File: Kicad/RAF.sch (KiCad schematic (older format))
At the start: 22 parts, among them P1 Power, P2 Analog, P3 Digital, P4 Digital, P5 CONN_01X01, P6 CONN_01X01, P7 CONN_01X01, P8 CONN_01X01, Q1 FDG1024NZ, U1 RGB_WS2811B

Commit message: add sot23-6 footprint, fix drc errors
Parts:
- removed Q1: FDG1024NZ, TO_SOT_Packages_SMD:SOT-363_SC-70-6, symbol FDG1024NZ
- added C1: 10uF 25V, symbol C
- added C2: 100n, symbol C
- added C3: 82pF, symbol C
- added C4, C5: 22uF, symbol C
- added J3: SOL, symbol CONN_01X02
- added J5: PUMP, symbol CONN_01X02
- added J6: WS2811-OUT, symbol CONN_01X03
- added L1: 12uH, symbol L
- added Q1: FDC6305N, TO_SOT_Packages_SMD:SuperSOT-6, symbol FDC6305N
- added R3, R7: 100K, symbol R
- added R4: 11K, symbol R
- added R5, R6: 10K, symbol R
- added S1: SPST-M, symbol SPST-M
- added U2: TPS54302, symbol TPS54302
- gave numbers to parts that had none: 3
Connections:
- wire segments 81 -> 130
- no-connect marks 5 -> 16
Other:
- note added: "Air pump control\n"
- note added: "Servo (6V - 2A) power supply"
- note added: "Solenoid Control"
- moved on the sheet: J1, J2, J4, JOY1, LDR1, P1, P2, P3, P4, P5, P6, P7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

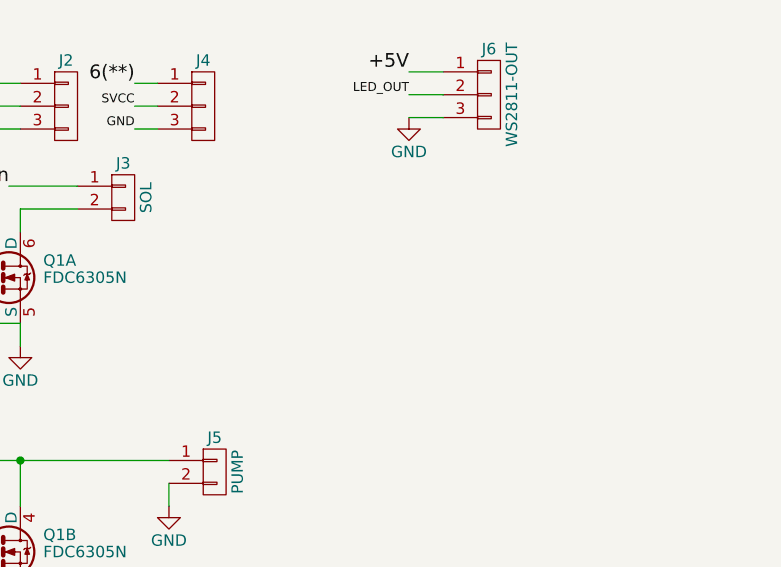
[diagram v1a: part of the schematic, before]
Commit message: add i2c header
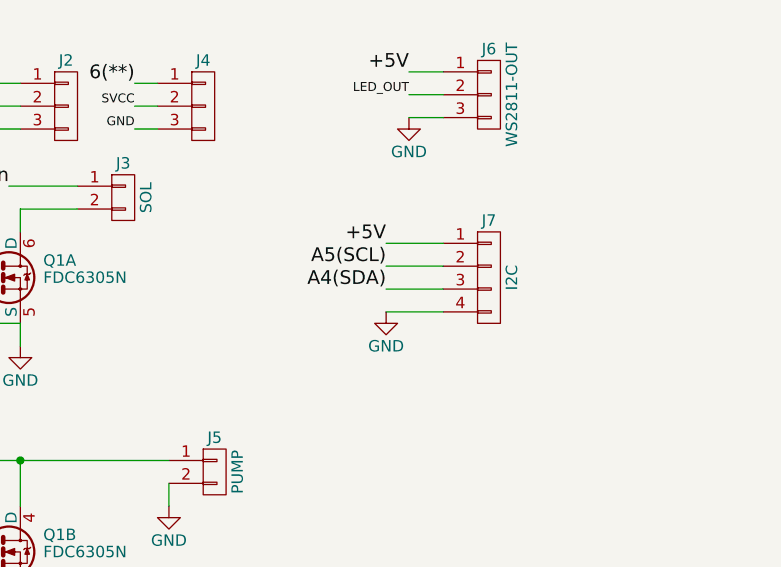
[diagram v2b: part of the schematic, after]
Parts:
- added J7: I2C, symbol CONN_01X04
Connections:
- net +5V: now also J7.1 (P1)
- net A4(SDA): now also J7.3 (P3)
- net A5(SCL): now also J7.2 (P2)
- net GND: now also J7.4 (P4)
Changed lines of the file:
@@
 $EndComp
 Connection ~ 8300 4550
+$Comp
+L CONN_01X04 J7
+U 1 1 59779033
+P 9250 1850
+F 0 "J7" H 9250 2100 50  0000 C CNN
+F 1 "I2C" V 9350 1850 50  0000 C CNN
+F 2 "" H 9250 1850 50  0001 C CNN
+F 3 "" H 9250 1850 50  0001 C CNN
+	1    9250 1850
+	1    0    0    -1
+$EndComp
+Wire Wire Line
+	8800 1700 9050 1700
+Wire Wire Line
+	9050 1800 8800 1800
+Wire Wire Line
+	8800 1900 9050 1900
+Wire Wire Line
+	9050 2000 8800 2000
+Text Label 8800 1800 2    60   ~ 0
+A5(SCL)
+Text Label 8800 1900 2    60   ~ 0
+A4(SDA)
+Text Label 8800 1700 2    60   ~ 0
++5V
+$Comp
+L GND #PWR022
+U 1 1 59779863
+P 8800 2000
+F 0 "#PWR022" H 8800 1750 50  0001 C CNN
+F 1 "GND" H 8800 1850 50  0000 C CNN
+F 2 "" H 8800 2000 50  0001 C CNN
+F 3 "" H 8800 2000 50  0001 C CNN
+	1    8800 2000
+	1    0    0    -1
+$EndComp
 $EndSCHEMATC

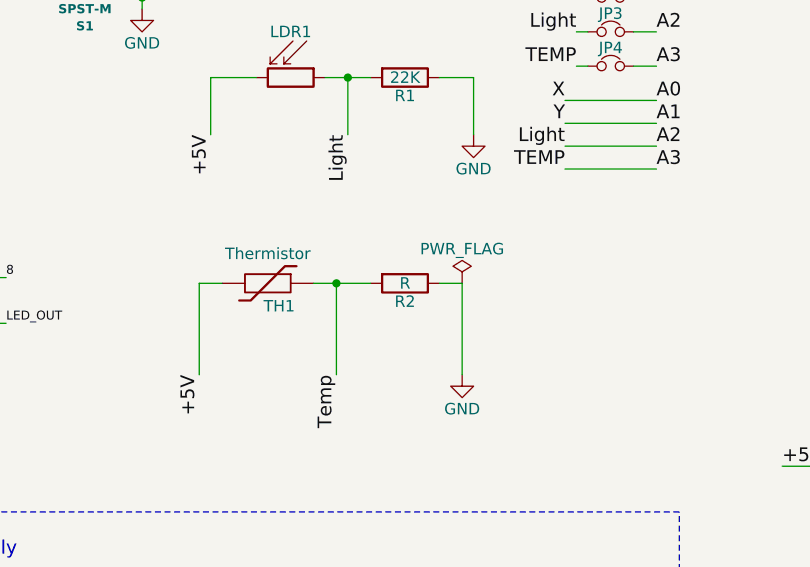
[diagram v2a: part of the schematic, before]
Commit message: update footprint allocation
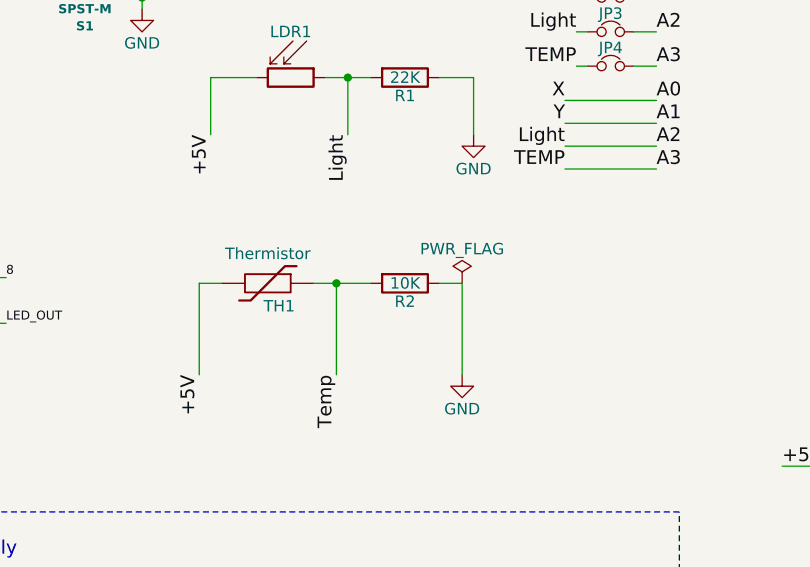
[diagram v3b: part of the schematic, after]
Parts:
- J1, J2, J4, J6: footprint (none) -> Pin_Headers:Pin_Header_Straight_1x03_Pitch2.54mm
- J5: footprint (none) -> Terminal_Blocks:TerminalBlock_Pheonix_PT-3.5mm_4pol
- J7: footprint (none) -> Pin_Headers:Pin_Header_Straight_1x04_Pitch2.54mm
- JOY1: footprint (none) -> RAF_Libs:Adafruit-thumb-joystick
- JP1, JP2, JP3, JP4: footprint (none) -> RAF_Libs:ShortLink2
- R2: value R -> 10K
- S1: footprint (none) -> Buttons_Switches_ThroughHole:SW_PUSH_6mm
- TH1: footprint (none) -> Resistors_SMD:R_0805_HandSoldering
- U1: footprint (none) -> LEDs:LED_WS2812B-PLCC4
- U2: footprint (none) -> TO_SOT_Packages_SMD:SOT-23-6
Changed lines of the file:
@@
 F 0 "JOY1" H 1000 1250 50  0000 C CNN
 F 1 "AnalogJoystick" H 1600 900 50  0000 C CNN
-F 2 "" V 1815 1400 50  0001 C CNN
+F 2 "RAF_Libs:Adafruit-thumb-joystick" V 1815 1400 50  0001 C CNN
 F 3 "" V 1815 1400 50  0001 C CNN
 	1    1600 1250
@@
 F 0 "TH1" V 3950 2350 50  0000 C CNN
 F 1 "Thermistor" V 3750 2300 50  0000 C BNN
-F 2 "" H 3850 2300 50  0001 C CNN
+F 2 "Resistors_SMD:R_0805_HandSoldering" H 3850 2300 50  0001 C CNN
 F 3 "" H 3850 2300 50  0001 C CNN
 	1    3850 2300
@@
 P 4450 2300
 F 0 "R2" V 4530 2300 50  0000 C CNN
-F 1 "R" V 4450 2300 50  0000 C CNN
+F 1 "10K" V 4450 2300 50  0000 C CNN
 F 2 "" V 4380 2300 50  0001 C CNN
 F 3 "" H 4450 2300 50  0001 C CNN
@@
 F 0 "JP1" H 5350 980 50  0000 C CNN
 F 1 "Jumper_NC_Small" H 5360 840 50  0001 C CNN
-F 2 "" H 5350 900 50  0001 C CNN
+F 2 "RAF_Libs:ShortLink2" H 5350 900 50  0001 C CNN
 F 3 "" H 5350 900 50  0001 C CNN
 	1    5350 900
@@
 F 0 "JP2" H 5350 1130 50  0000 C CNN
 F 1 "Jumper_NC_Small" H 5360 990 50  0001 C CNN
-F 2 "" H 5350 1050 50  0001 C CNN
+F 2 "RAF_Libs:ShortLink2" H 5350 1050 50  0001 C CNN
 F 3 "" H 5350 1050 50  0001 C CNN
 	1    5350 1050
@@
 F 0 "JP3" H 5350 1280 50  0000 C CNN
 F 1 "Jumper_NC_Small" H 5360 1140 50  0001 C CNN
-F 2 "" H 5350 1200 50  0001 C CNN
+F 2 "RAF_Libs:ShortLink2" H 5350 1200 50  0001 C CNN
 F 3 "" H 5350 1200 50  0001 C CNN
 	1    5350 1200
@@
 F 0 "JP4" H 5350 1430 50  0000 C CNN
 F 1 "Jumper_NC_Small" H 5360 1290 50  0001 C CNN
-F 2 "" H 5350 1350 50  0001 C CNN
+F 2 "RAF_Libs:ShortLink2" H 5350 1350 50  0001 C CNN
 F 3 "" H 5350 1350 50  0001 C CNN
 	1    5350 1350
@@
 F 0 "J2" H 7400 1300 50  0000 C CNN
 F 1 "CONN_01X03" V 7500 1100 50  0001 C CNN
-F 2 "" H 7400 1100 50  0001 C CNN
+F 2 "Pin_Headers:Pin_Header_Straight_1x03_Pitch2.54mm" H 7400 1100 50  0001 C CNN
 F 3 "" H 7400 1100 50  0001 C CNN
 	1    7400 1100
@@
 F 0 "J1" H 6800 1300 50  0000 C CNN
 F 1 "CONN_01X03" V 6900 1100 50  0001 C CNN
-F 2 "" H 6800 1100 50  0001 C CNN
+F 2 "Pin_Headers:Pin_Header_Straight_1x03_Pitch2.54mm" H 6800 1100 50  0001 C CNN
 F 3 "" H 6800 1100 50  0001 C CNN
 	1    6800 1100
@@
 F 0 "J4" H 8000 1300 50  0000 C CNN
 F 1 "CONN_01X03" V 8100 1100 50  0001 C CNN
-F 2 "" H 8000 1100 50  0001 C CNN
+F 2 "Pin_Headers:Pin_Header_Straight_1x03_Pitch2.54mm" H 8000 1100 50  0001 C CNN
 F 3 "" H 8000 1100 50  0001 C CNN
 	1    8000 1100
@@
 F 0 "U1" V 1800 2200 60  0000 C CNN
 F 1 "RGB_WS2811B" V 2450 2200 60  0000 C CNN
-F 2 "" H 2050 2200 60  0000 C CNN
+F 2 "LEDs:LED_WS2812B-PLCC4" H 2050 2200 60  0001 C CNN
 F 3 "" H 2050 2200 60  0000 C CNN
 	1    2050 2200
@@
 F 0 "J5" H 8050 2850 50  0000 C CNN
 F 1 "PUMP" V 8150 2700 50  0000 C CNN
-F 2 "" H 8050 2700 50  0001 C CNN
+F 2 "Terminal_Blocks:TerminalBlock_Pheonix_PT-3.5mm_4pol" H 8050 2700 50  0001 C CNN
 F 3 "" H 8050 2700 50  0001 C CNN
 	1    8050 2700
@@
 F 0 "U2" H 2700 3800 60  0000 C CNN
 F 1 "TPS54302" H 2700 4150 60  0000 C CNN
-F 2 "" H 2700 3900 60  0001 C CNN
+F 2 "TO_SOT_Packages_SMD:SOT-23-6" H 2700 3900 60  0001 C CNN
 F 3 "" H 2700 3900 60  0001 C CNN
 	1    2700 3900
@@
 F 0 "S1" H 3050 825 40  0000 C CNB
 F 1 "SPST-M" H 3050 900 40  0000 C CNB
-F 2 "" H 3050 1000 60  0000 C CNN
+F 2 "Buttons_Switches_ThroughHole:SW_PUSH_6mm" H 3050 1000 60  0001 C CNN
 F 3 "" H 3050 1000 60  0000 C CNN
 	1    3050 1000
@@
 F 0 "J6" H 9250 1250 50  0000 C CNN
 F 1 "WS2811-OUT" V 9350 1050 50  0000 C CNN
-F 2 "" H 9250 1050 50  0001 C CNN
+F 2 "Pin_Headers:Pin_Header_Straight_1x03_Pitch2.54mm" H 9250 1050 50  0001 C CNN
 F 3 "" H 9250 1050 50  0001 C CNN
 	1    9250 1050
@@
 F 0 "J7" H 9250 2100 50  0000 C CNN
 F 1 "I2C" V 9350 1850 50  0000 C CNN
-F 2 "" H 9250 1850 50  0001 C CNN
+F 2 "Pin_Headers:Pin_Header_Straight_1x04_Pitch2.54mm" H 9250 1850 50  0001 C CNN
 F 3 "" H 9250 1850 50  0001 C CNN
 	1    9250 1850
